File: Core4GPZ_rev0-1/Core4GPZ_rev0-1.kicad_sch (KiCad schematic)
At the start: 6 parts, among them U2 core4, U3 MPXHZ6250AC6T1

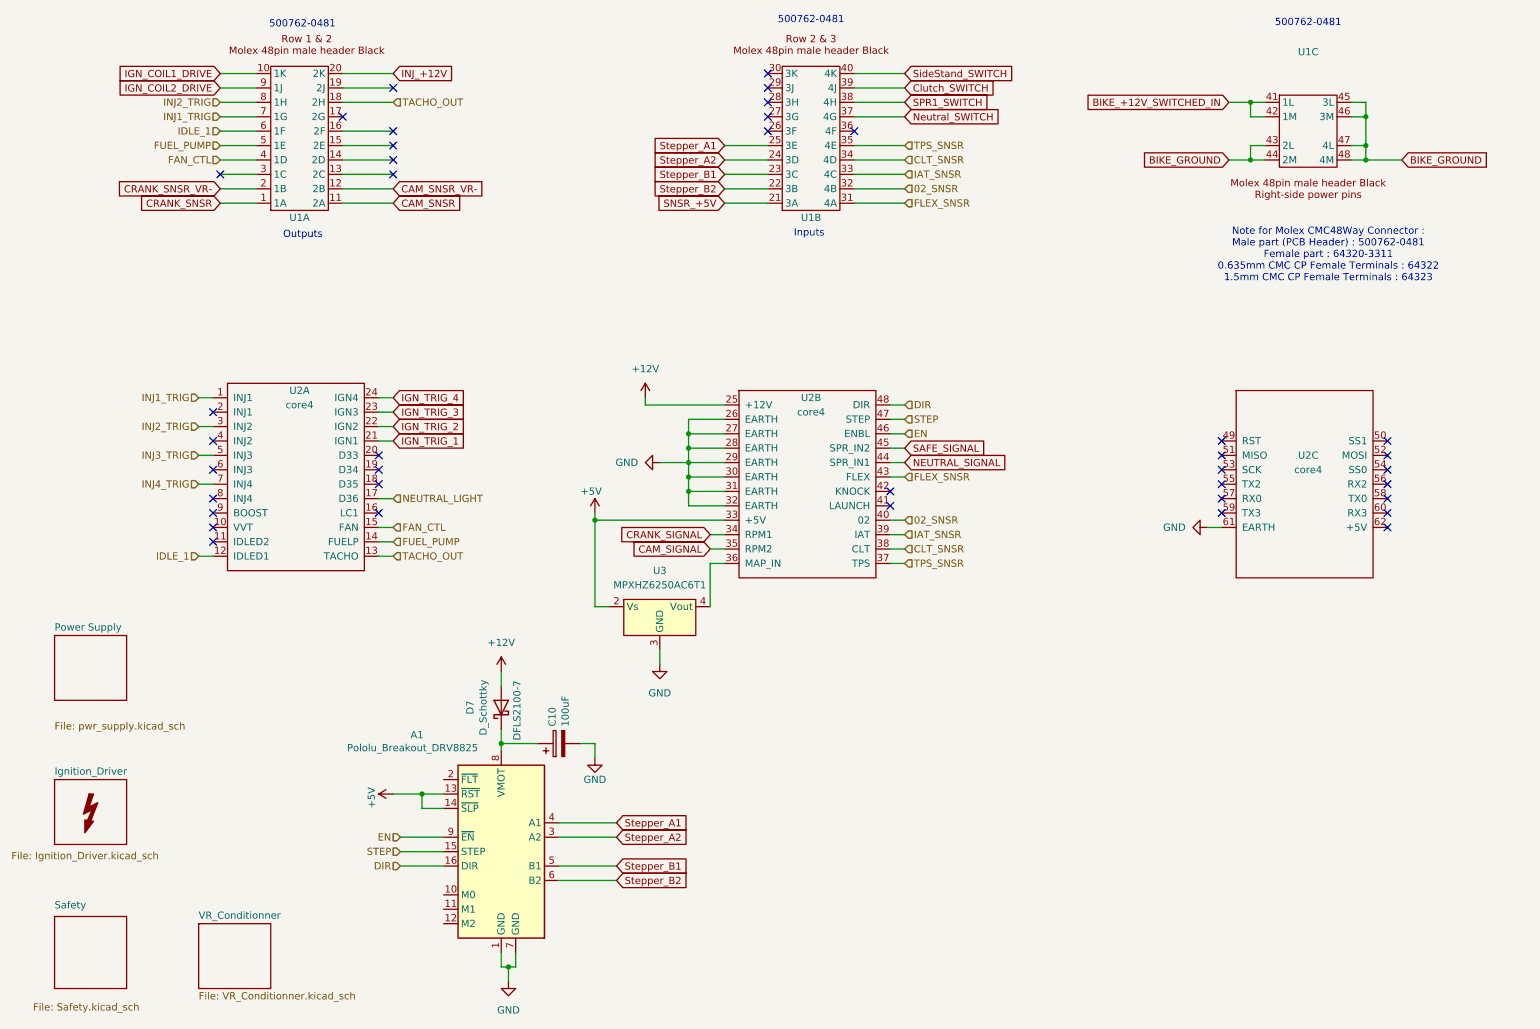
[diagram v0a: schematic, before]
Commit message: Implemented DRV8825 and upgrade IGN Driver
Ignition drivers upgraded with SMD IGBT FGD3440
Added Stepper Driver DRV8825
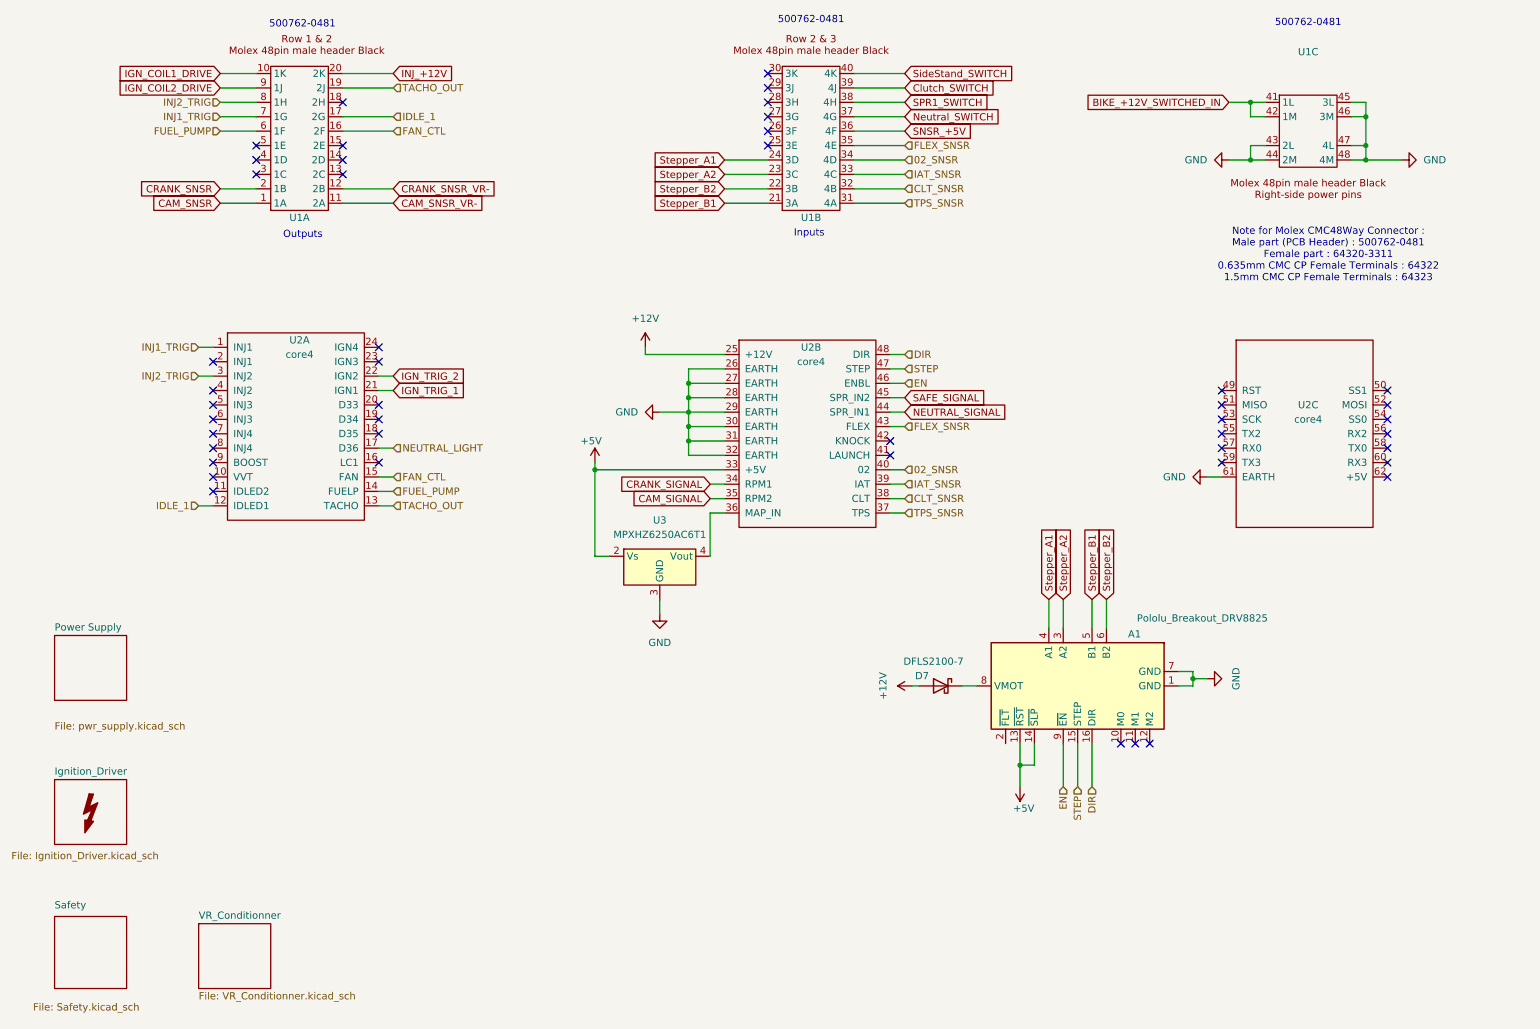
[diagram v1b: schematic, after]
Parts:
- removed C10: 100uF, Capacitor_SMD:CP_Elec_6.3x7.7, symbol Device:CP
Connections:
- net BIKE_GROUND is gone; now on net GND: U1.43 (2L), U1.44 (2M), U1.45 (3L), U1.46 (3M), U1.47 (4L), U1.48 (4M)
- net 02_SNSR: now also U1.34 (4D); no longer U1.32 (4B)
- net CAM_SNSR: now also U1.1 (1A); no longer U1.11 (2A)
- net CAM_SNSR_VR-: now also U1.11 (2A); no longer U1.12 (2B)
- net CLT_SNSR: now also U1.32 (4B); no longer U1.34 (4D)
- net CRANK_SNSR: now also U1.2 (1B); no longer U1.1 (1A)
- net CRANK_SNSR_VR-: now also U1.12 (2B); no longer U1.2 (1B)
- net FAN_CTL: now also U1.16 (2F); no longer U1.4 (1D)
- net FLEX_SNSR: now also U1.35 (4E); no longer U1.31 (4A)
- net FUEL_PUMP: now also U1.6 (1F); no longer U1.5 (1E)
- net IDLE_1: now also U1.17 (2G); no longer U1.6 (1F)
- net SNSR_+5V: now also U1.36 (4F); no longer U1.21 (3A)
- net Stepper_A1: now also U1.24 (3D); no longer U1.25 (3E)
- net Stepper_A2: now also U1.23 (3C); no longer U1.24 (3D)
- net Stepper_B1: now also U1.21 (3A); no longer U1.23 (3C)
- net TACHO_OUT: now also U1.19 (2J); no longer U1.18 (2H)
- net TPS_SNSR: now also U1.31 (4A); no longer U1.35 (4E)
- net IGN_TRIG_3: no longer names the net of U2.23 (IGN3)
- net IGN_TRIG_4: no longer names the net of U2.24 (IGN4)
- net INJ3_TRIG: no longer names the net of U2.5 (INJ3)
- net INJ4_TRIG: no longer names the net of U2.7 (INJ4)
- no-connect marks 39 -> 46
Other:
- moved on the sheet: A1, U2A, U2B, U2C, U3

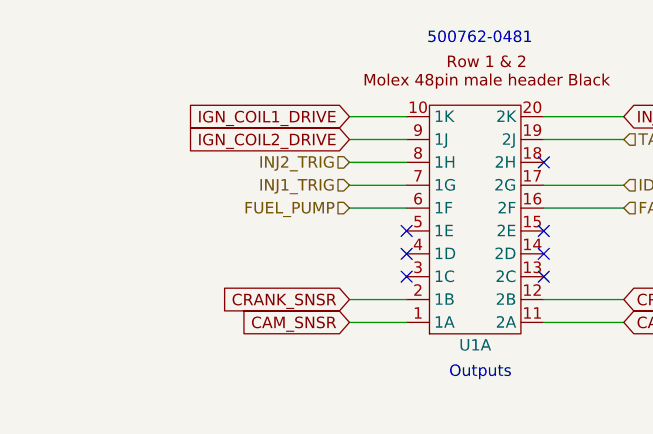
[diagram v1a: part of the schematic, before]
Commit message: Reduced board width
moved IGN Driver under the Core4 to reduce overall board size
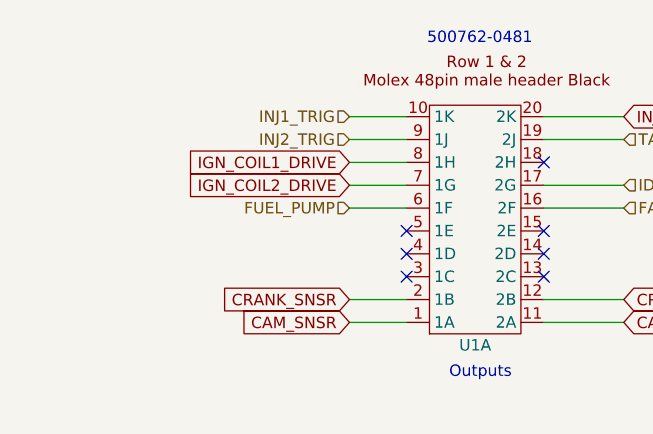
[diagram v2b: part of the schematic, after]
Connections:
- net IGN_COIL1_DRIVE: now also U1.8 (1H); no longer U1.10 (1K)
- net IGN_COIL2_DRIVE: now also U1.7 (1G); no longer U1.9 (1J)
- net INJ1_TRIG: now also U1.10 (1K); no longer U1.7 (1G)
- net INJ2_TRIG: now also U1.9 (1J); no longer U1.8 (1H)

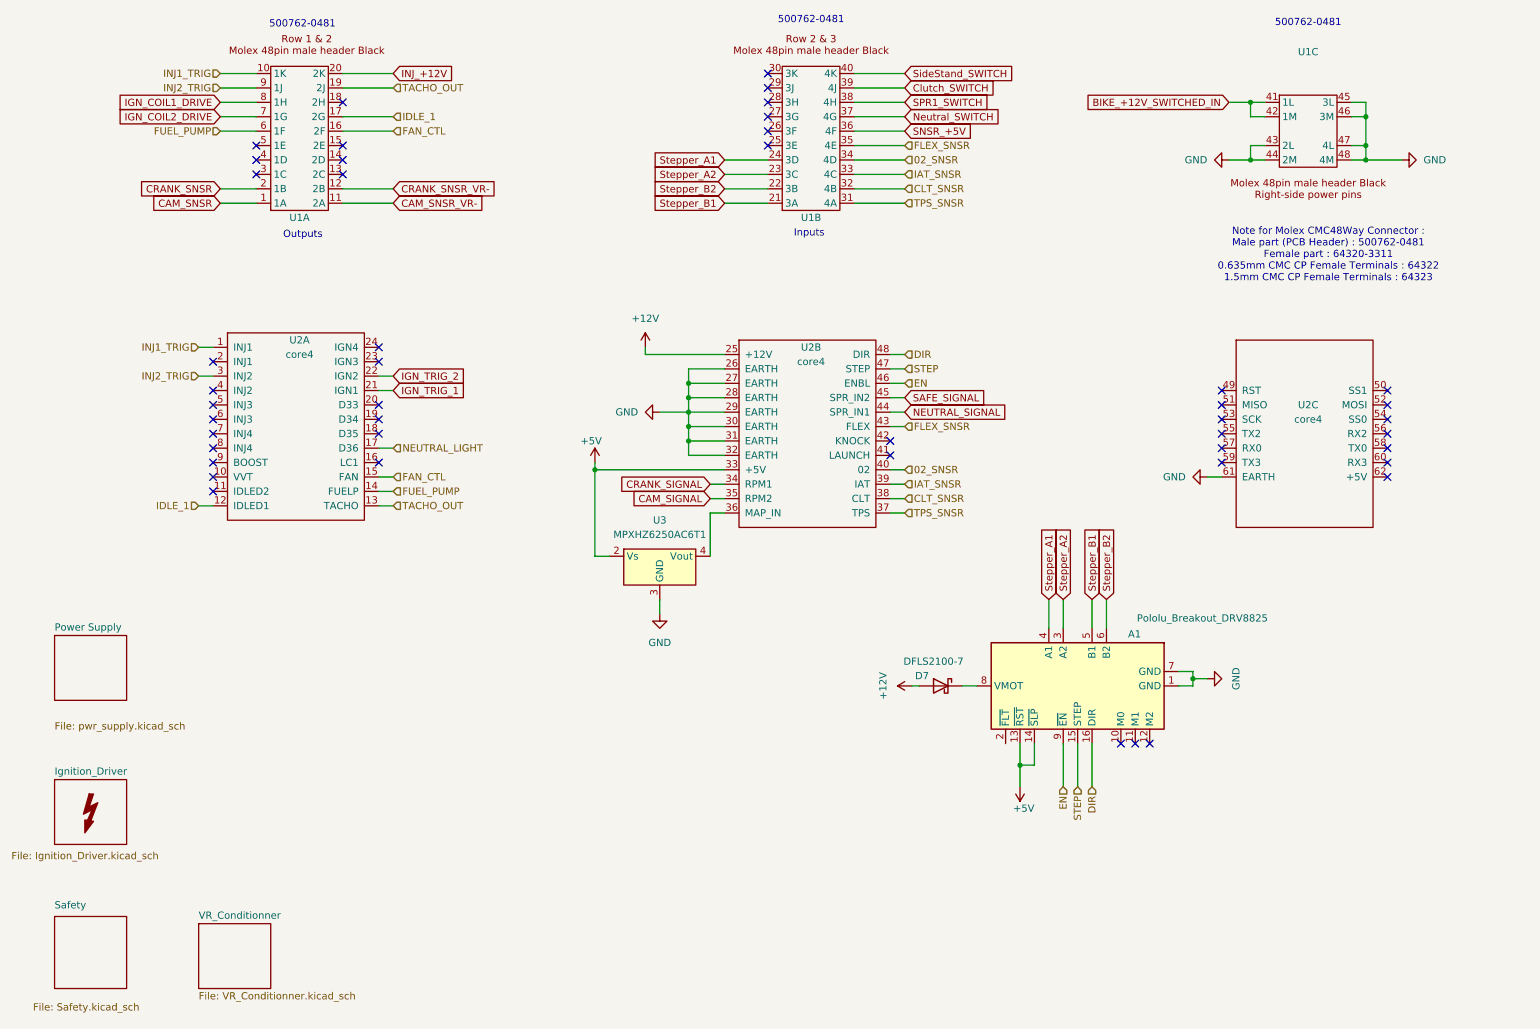
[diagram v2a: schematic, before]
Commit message: Added AOP for a proper decoupling for CLT
Modified Fixing point and dimensions on the enclosure
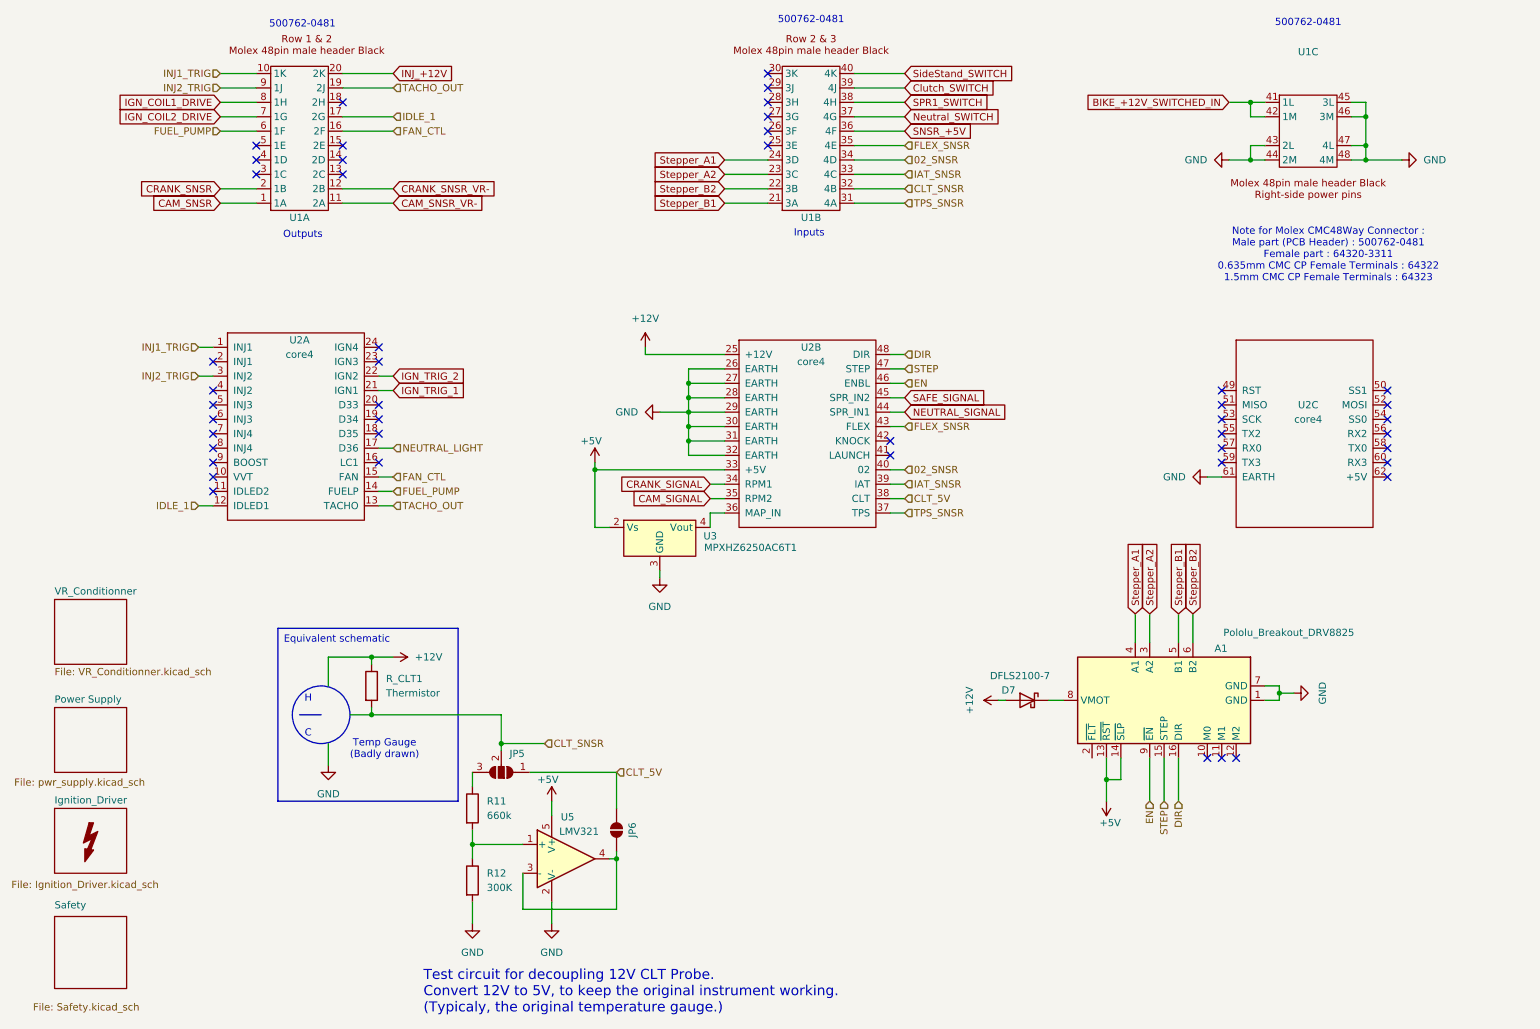
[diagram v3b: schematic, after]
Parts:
- added JP5: SolderJumper_3_Open, Jumper:SolderJumper-3_P1.3mm_Open_RoundedPad1.0x1.5mm, symbol Jumper:SolderJumper_3_Open
- added JP6: SolderJumper_2_Open, Jumper:SolderJumper-2_P1.3mm_Open_RoundedPad1.0x1.5mm, symbol Jumper:SolderJumper_2_Open
- added R11: 660k, Resistor_SMD:R_0805_2012Metric_Pad1.20x1.40mm_HandSolder, symbol Device:R
- added R12: 300K, Resistor_SMD:R_0805_2012Metric_Pad1.20x1.40mm_HandSolder, symbol Device:R
- added R_CLT1: Thermistor, symbol Device:R
- added U5: LMV321, Package_TO_SOT_SMD:SOT-23-5_HandSoldering, symbol Amplifier_Operational:LMV321
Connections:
- net +12V: now also R_CLT1.1
- net +5V: now also U5.5 (V+)
- net CLT_SNSR: now also JP5.2 (C), R_CLT1.2; no longer U2.38 (CLT)
- net GND: now also R12.2, U5.2 (V-)
- new net: JP5.3 (B), R11.1
- new net: R11.2, R12.1, U5.1 (+)
- new net: JP6.2 (B), U5.3 (-), U5.4
- new net CLT_5V: JP5.1 (A), JP6.1 (A), U2.38 (CLT)
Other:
- note added: "H C"
- note added: "Temp Gauge (Badly drawn)"
- note added: "Test circuit for decoupling 12V CLT Probe. Convert 12V to 5V, to keep the original instrument working. (Typicaly, the original temperature gauge.)"
- moved on the sheet: A1, D7, U3

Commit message: Removed NeutralSwitch. Added Up-Shifter support
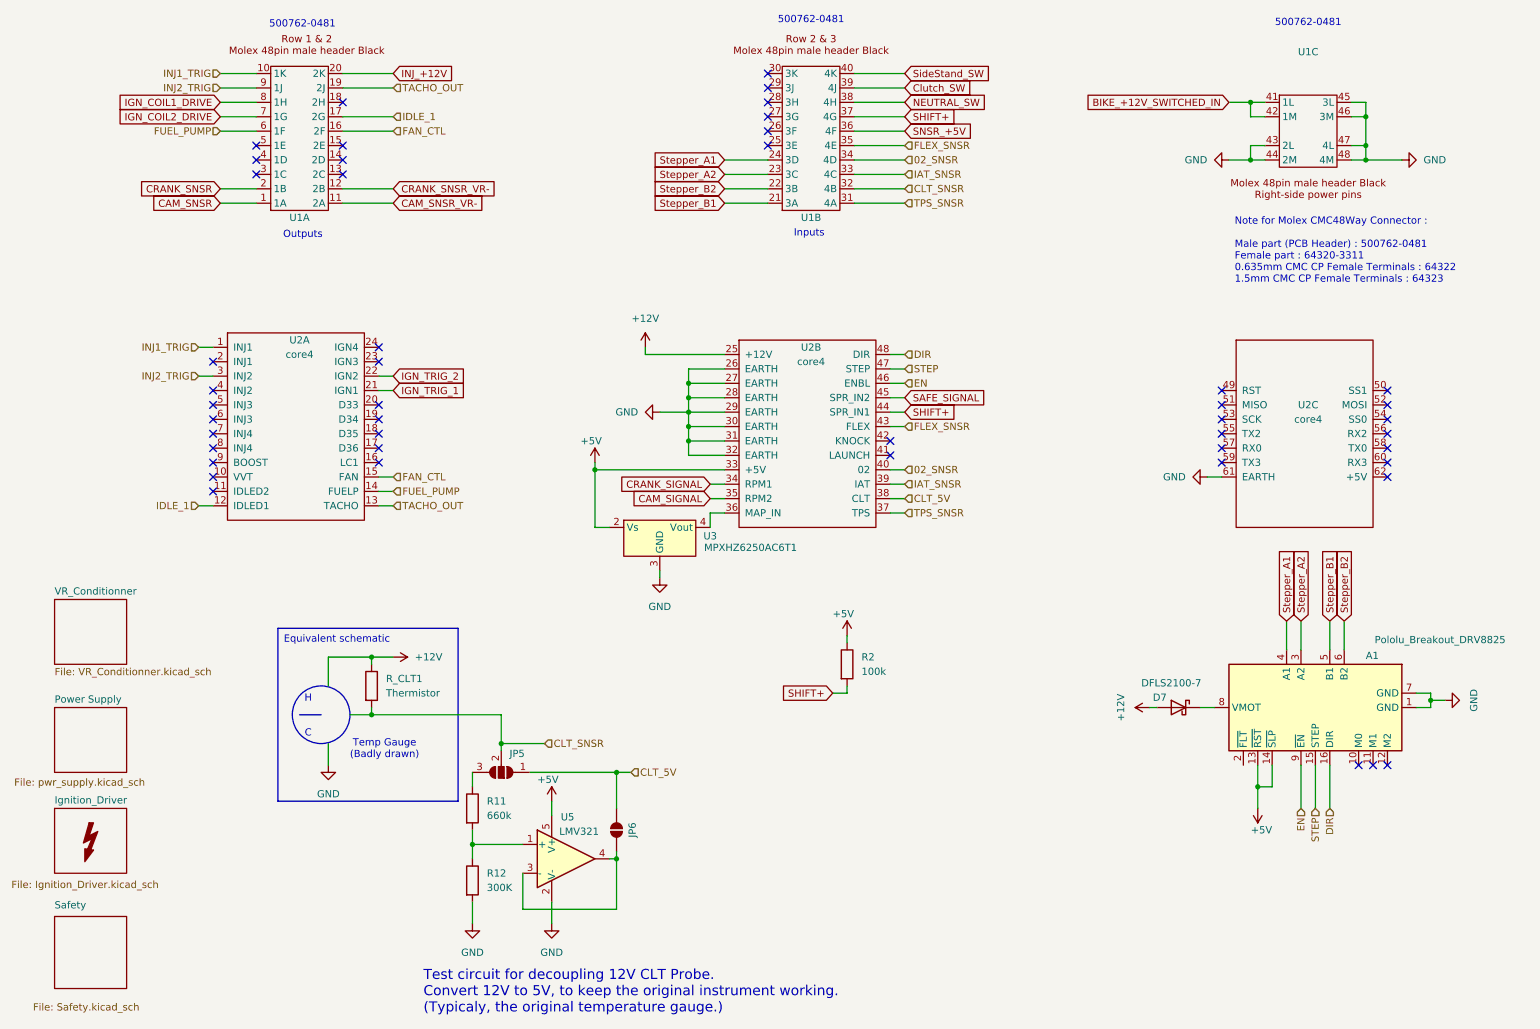
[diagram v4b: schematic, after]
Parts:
- added R2: 100k, Resistor_SMD:R_0603_1608Metric, symbol Device:R
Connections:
- net Neutral_SWITCH is gone; now on net SHIFT+: U1.37 (4G)
- net +5V: now also R2.1
- net Clutch_SWITCH renamed Clutch_SW
- net NEUTRAL_LIGHT: no longer names the net of U2.17 (D36)
- net NEUTRAL_SIGNAL renamed SHIFT+
- net SHIFT+: now also R2.2
- net SPR1_SWITCH renamed NEUTRAL_SW
- net SideStand_SWITCH renamed SideStand_SW
- no-connect marks 46 -> 47
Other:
- moved on the sheet: A1, D7

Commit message: Reorganised Schematic
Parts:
- removed A1: Pololu_Breakout_DRV8825, Module:Pololu_Breakout-16_15.2x20.3mm, symbol Driver_Motor:Pololu_Breakout_DRV8825
- removed D7: D_Schottky, Diode_SMD:D_PowerDI-123, symbol Device:D_Schottky
- removed JP5: SolderJumper_3_Open, Jumper:SolderJumper-3_P1.3mm_Open_RoundedPad1.0x1.5mm, symbol Jumper:SolderJumper_3_Open
- removed JP6: SolderJumper_2_Open, Jumper:SolderJumper-2_P1.3mm_Open_RoundedPad1.0x1.5mm, symbol Jumper:SolderJumper_2_Open
- removed R11: 660k, Resistor_SMD:R_0805_2012Metric_Pad1.20x1.40mm_HandSolder, symbol Device:R
- removed R12: 300K, Resistor_SMD:R_0805_2012Metric_Pad1.20x1.40mm_HandSolder, symbol Device:R
- removed R_CLT1: Thermistor, symbol Device:R
- removed U5: LMV321, Package_TO_SOT_SMD:SOT-23-5_HandSoldering, symbol Amplifier_Operational:LMV321
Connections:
- no-connect marks 47 -> 44
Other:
- sheet Ignition_Driver renamed Output Drivers
- sheet Safety renamed Inputs
- removed sheet Power Supply
- sheet Inputs: file Safety.kicad_sch -> inputs.kicad_sch
- sheet Output Drivers: file Ignition_Driver.kicad_sch -> output_driver.kicad_sch
- note removed: "H C"
- note removed: "Temp Gauge (Badly drawn)"
- note removed: "Test circuit for decoupling 12V CLT Probe. Convert 12V to 5V, to keep the original instrument working. (Typicaly, the original temperature gauge.)"
- moved on the sheet: R2, U1A, U1B, U1C, U2A, U2B, U2C, U3

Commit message: Updated CAD Enclosure STL and STEP export
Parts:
- R2: footprint Resistor_SMD:R_0603_1608Metric -> Resistor_SMD:R_0603_1608Metric_Pad0.98x0.95mm_HandSolder
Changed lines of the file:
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@@
 			)
 		)
-		(property "Footprint" "Resistor_SMD:R_0603_1608Metric"
+		(property "Footprint" "Resistor_SMD:R_0603_1608Metric_Pad0.98x0.95mm_HandSolder"
 			(at 205.232 93.98 90)
 			(effects
